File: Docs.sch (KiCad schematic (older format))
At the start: 0 parts

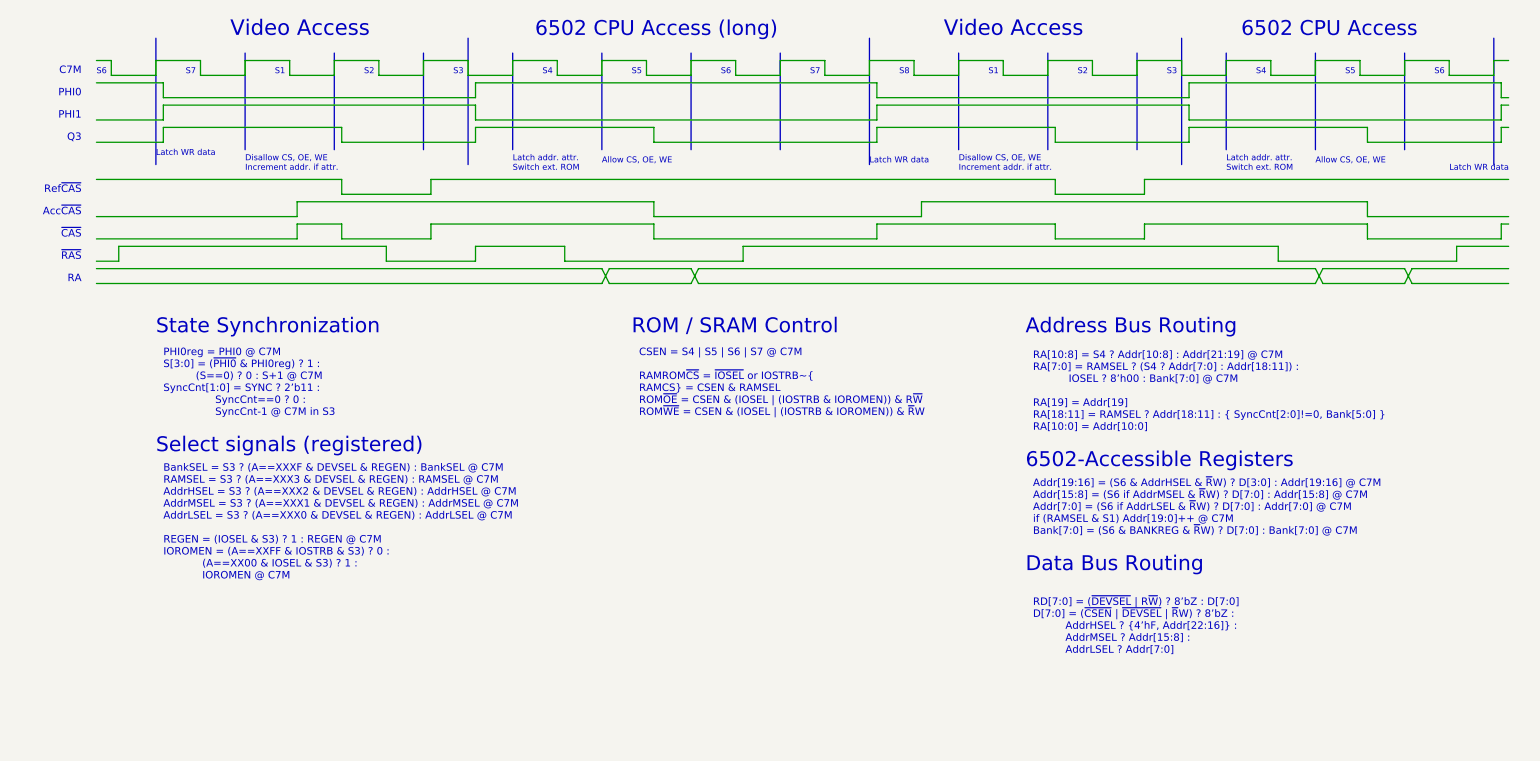
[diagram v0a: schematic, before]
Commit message: Buffered data bus with CPLD
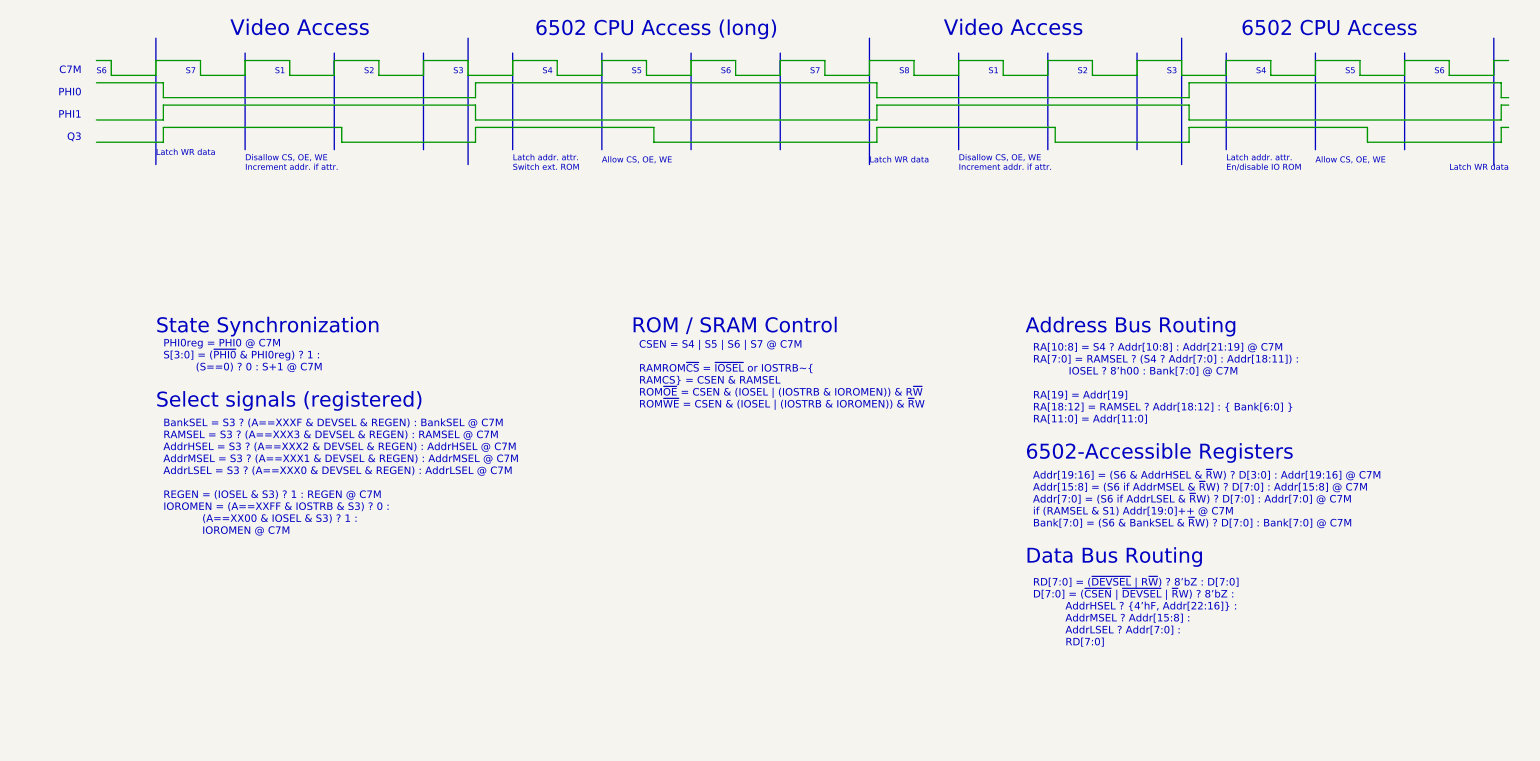
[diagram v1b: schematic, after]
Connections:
- wire segments 176 -> 106
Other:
- note added: "Addr[19:16] = (S6 & AddrHSEL & ~R~W) ? D[3:0] : Addr[19:16] @ C7M\nAddr[15:8] = (S6 if AddrMSEL & ~R~W) ? D[7:0] : Addr[15:8] @ C7M\nAddr[7:0] = (S6 if AddrLSEL & ~R~W) ? D[7:0] : Addr[7:0] @ C7M\nif (RAMSEL & S1) Addr[19:0]++ @ C7M\nBank[7:0] = (S6 & BankSEL & ~R~W) ? D[7:0] : Bank[7:0] @ C7M"
- note added: "Latch addr. attr.\nEn/disable IO ROM"
- note added: "PHI0reg = PHI0 @ C7M\nS[3:0] = (~PHI0~ & PHI0reg) ? 1 : \n (S==0) ? 0 : S+1 @ C7M"
- note added: "RA[10:8] = S4 ? Addr[10:8] : Addr[21:19] @ C7M\nRA[7:0] = RAMSEL ? (S4 ? Addr[7:0] : Addr[18:11]) : \n IOSEL ? 8’h00 : Bank[7:0] @ C7M\n\nRA[19] = Addr[19]\nRA[18:12] = RAMSEL ? Addr[18:12] : { Bank[6:0] }\nRA[11:0] = Addr[11:0]"
- note added: "RD[7:0] = (~DEVSEL~ | R~W~) ? 8’bZ : D[7:0]\nD[7:0] = (~CSEN~ | ~DEVSEL~ | ~R~W) ? 8’bZ :\n AddrHSEL ? {4’hF, Addr[22:16]} : \n AddrMSEL ? Addr[15:8] : \n AddrLSEL ? Addr[7:0] :\n RD[7:0]"
- note removed: "Acc~CAS~"
- note removed: "Addr[19:16] = (S6 & AddrHSEL & ~R~W) ? D[3:0] : Addr[19:16] @ C7M\nAddr[15:8] = (S6 if AddrMSEL & ~R~W) ? D[7:0] : Addr[15:8] @ C7M\nAddr[7:0] = (S6 if AddrLSEL & ~R~W) ? D[7:0] : Addr[7:0] @ C7M\nif (RAMSEL & S1) Addr[19:0]++ @ C7M\nBank[7:0] = (S6 & BANKREG & ~R~W) ? D[7:0] : Bank[7:0] @ C7M"
- note removed: "PHI0reg = PHI0 @ C7M\nS[3:0] = (~PHI0~ & PHI0reg) ? 1 : \n (S==0) ? 0 : S+1 @ C7M\nSyncCnt[1:0] = SYNC ? 2’b11 : \n SyncCnt==0 ? 0 :\n SyncCnt-1 @ C7M in S3"
- note removed: "RA"
- note removed: "RA[10:8] = S4 ? Addr[10:8] : Addr[21:19] @ C7M\nRA[7:0] = RAMSEL ? (S4 ? Addr[7:0] : Addr[18:11]) : \n IOSEL ? 8’h00 : Bank[7:0] @ C7M\n\nRA[19] = Addr[19]\nRA[18:11] = RAMSEL ? Addr[18:11] : { SyncCnt[2:0]!=0, Bank[5:0] }\nRA[10:0] = Addr[10:0]"
- note removed: "RD[7:0] = (~DEVSEL~ | R~W~) ? 8’bZ : D[7:0]\nD[7:0] = (~CSEN~ | ~DEVSEL~ | ~R~W) ? 8’bZ :\n AddrHSEL ? {4’hF, Addr[22:16]} : \n AddrMSEL ? Addr[15:8] : \n AddrLSEL ? Addr[7:0]"
- note removed: "Ref~CAS~"
- note removed: "~CAS~"
- note removed: "~RAS~"
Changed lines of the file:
@@
 Comment4 ""
 $EndDescr
-Wire Wire Line
-	8850 2250 8850 2350
-Wire Wire Line
-	9450 1950 9450 2050
-Wire Wire Line
-	4650 1950 4650 2050
-Wire Wire Line
-	4050 2350 4050 2250
-Text Notes 800  2050 2    50   ~ 0
-Acc~CAS~
-Wire Wire Line
-	3150 1900 2550 1900
 Wire Bus Line
 	4300 950  4300 1600
@@
 Text Notes 4300 1700 0    40   ~ 0
 Allow CS, OE, WE
-Text Notes 3700 1750 0    40   ~ 0
-Latch addr. attr.\nSwitch ext. ROM
-Text Notes 800  2350 2    50   ~ 0
-~RAS~
-Text Notes 800  1900 2    50   ~ 0
-Ref~CAS~
 Text Notes 1500 1100 0    40   ~ 0
 S7
@@
 Text Notes 9900 1100 0    40   ~ 0
 S6
-Text Notes 8500 1750 0    40   ~ 0
-Latch addr. attr.\nSwitch ext. ROM
-Text Notes 6700 1750 0    40   ~ 0
-Disallow CS, OE, WE\nIncrement addr. if attr.
 Wire Wire Line
 	6150 1250 8250 1250
@@
 Wire Bus Line
 	1300 850  1300 1700
-Wire Wire Line
-	7350 1800 7350 1900
-Wire Wire Line
-	3150 1900 3150 1800
-Wire Wire Line
-	2550 1800 2550 1900
-Wire Wire Line
-	3450 2350 3450 2250
-Wire Wire Line
-	2850 2350 3450 2350
-Wire Wire Line
-	2850 2250 2850 2350
-Text Notes 1900 1750 0    40   ~ 0
-Disallow CS, OE, WE\nIncrement addr. if attr.
 Text Notes 1300 1650 0    40   ~ 0
 Latch WR data
@@
 Wire Wire Line
 	5200 1000 5200 1100
-Wire Wire Line
-	9700 2400 9750 2500
-Wire Wire Line
-	9700 2500 9750 2400
-Wire Wire Line
-	9150 2500 9700 2500
-Wire Wire Line
-	9150 2400 9700 2400
-Wire Wire Line
-	9100 2500 9150 2400
-Wire Wire Line
-	9100 2400 9150 2500
-Wire Wire Line
-	9100 2500 4950 2500
-Wire Wire Line
-	4950 2400 9100 2400
-Wire Wire Line
-	4900 2400 4950 2500
-Wire Wire Line
-	4900 2500 4950 2400
-Wire Wire Line
-	4350 2500 4900 2500
-Wire Wire Line
-	4350 2400 4900 2400
-Wire Wire Line
-	4300 2500 4350 2400
-Wire Wire Line
-	4300 2400 4350 2500
-Wire Wire Line
-	900  2400 4300 2400
-Wire Wire Line
-	4300 2500 900  2500
-Text Notes 800  2500 2    50   ~ 0
-RA
-Wire Wire Line
-	2250 2050 2250 1950
-Wire Wire Line
-	2250 1950 4650 1950
-Wire Wire Line
-	5250 2350 5250 2250
-Wire Wire Line
-	5250 2250 8850 2250
-Wire Wire Line
-	1050 2350 1050 2250
-Wire Wire Line
-	1050 2250 2850 2250
-Wire Wire Line
-	900  2350 1050 2350
-Wire Wire Line
-	8850 2350 10050 2350
-Wire Wire Line
-	10050 2350 10050 2250
-Wire Wire Line
-	3450 2250 4050 2250
-Wire Wire Line
-	7950 1900 7950 1800
-Wire Wire Line
-	7950 1900 7350 1900
-Wire Wire Line
-	9450 2100 9450 2200
-Wire Wire Line
-	4650 2100 4650 2200
-Text Notes 800  2200 2    50   ~ 0
-~CAS~
-Wire Wire Line
-	2250 2200 2250 2100
-Wire Wire Line
-	3150 2200 3150 2100
-Wire Wire Line
-	2550 2100 2550 2200
-Wire Wire Line
-	2250 2100 2550 2100
-Wire Wire Line
-	7350 2100 7350 2200
-Wire Wire Line
-	7950 2200 7950 2100
-Wire Wire Line
-	7950 2200 7350 2200
-Wire Wire Line
-	7950 2100 9450 2100
-Wire Wire Line
-	4650 2200 6150 2200
-Wire Wire Line
-	6150 2200 6150 2100
-Wire Wire Line
-	6150 2100 7350 2100
-Wire Wire Line
-	9450 2200 10350 2200
-Wire Wire Line
-	10350 2200 10350 2100
-Wire Wire Line
-	4650 2050 6450 2050
-Wire Wire Line
-	6450 2050 6450 1950
-Wire Wire Line
-	6450 1950 9450 1950
-Wire Wire Line
-	900  2200 2250 2200
-Wire Wire Line
-	900  2050 2250 2050
-Wire Wire Line
-	3150 1800 7350 1800
-Wire Wire Line
-	900  1800 2550 1800
-Wire Wire Line
-	3150 2100 4650 2100
-Wire Wire Line
-	2550 2200 3150 2200
-Wire Wire Line
-	4050 2350 5250 2350
-Text Notes 4550 3400 0    50   ~ 0
+Text Notes 4550 3350 0    50   ~ 0
 CSEN = S4 | S5 | S6 | S7 @ C7M\n\nRAMROM~CS~ = ~IOSEL or IOSTRB~\nRAMCS = CSEN & RAMSEL\nROM~OE~ = CSEN & (IOSEL | (IOSTRB & IOROMEN)) & R~W~\nROM~WE~ = CSEN & (IOSEL | (IOSTRB & IOROMEN)) & ~R~W
-Text Notes 1350 3400 0    50   ~ 0
-PHI0reg = PHI0 @ C7M\nS[3:0] = (~PHI0~ & PHI0reg) ? 1 : \n          (S==0) ? 0 : S+1 @ C7M\nSyncCnt[1:0] = SYNC ? 2’b11 : \n                SyncCnt==0 ? 0 :\n                SyncCnt-1 @ C7M in S3
-Text Notes 7200 3500 0    50   ~ 0
-RA[10:8] = S4 ? Addr[10:8] : Addr[21:19] @ C7M\nRA[7:0] = RAMSEL ? (S4 ? Addr[7:0] : Addr[18:11]) : \n           IOSEL ? 8’h00 : Bank[7:0] @ C7M\n\nRA[19] = Addr[19]\nRA[18:11] = RAMSEL ? Addr[18:11] : { SyncCnt[2:0]!=0, Bank[5:0] }\nRA[10:0] = Addr[10:0]
-Text Notes 1300 3650 0    100  ~ 0
+Text Notes 1350 3100 0    50   ~ 0
+PHI0reg = PHI0 @ C7M\nS[3:0] = (~PHI0~ & PHI0reg) ? 1 : \n          (S==0) ? 0 : S+1 @ C7M
+Text Notes 1300 3350 0    100  ~ 0
 Select signals (registered)
 Text Notes 1300 2850 0    100  ~ 0
@@
 Text Notes 4500 2850 0    100  ~ 0
 ROM / SRAM Control
-Text Notes 1350 4500 0    50   ~ 0
+Text Notes 1350 4200 0    50   ~ 0
 BankSEL = S3 ? (A==XXXF & DEVSEL & REGEN) : BankSEL @ C7M\nRAMSEL = S3 ? (A==XXX3 & DEVSEL & REGEN) : RAMSEL @ C7M\nAddrHSEL = S3 ? (A==XXX2 & DEVSEL & REGEN) : AddrHSEL @ C7M\nAddrMSEL = S3 ? (A==XXX1 & DEVSEL & REGEN) : AddrMSEL @ C7M\nAddrLSEL = S3 ? (A==XXX0 & DEVSEL & REGEN) : AddrLSEL @ C7M\n\nREGEN = (IOSEL & S3) ? 1 : REGEN @ C7M\nIOROMEN = (A==XXFF & IOSTRB & S3) ? 0 :\n            (A==XX00 & IOSEL & S3) ? 1 :\n            IOROMEN @ C7M
 Text Notes 7150 2850 0    100  ~ 0
 Address Bus Routing
-Text Notes 7150 3750 0    100  ~ 0
+Text Notes 7150 3700 0    100  ~ 0
 6502-Accessible Registers
-Text Notes 7200 4200 0    50   ~ 0
-Addr[19:16] = (S6 & AddrHSEL & ~R~W) ? D[3:0] : Addr[19:16] @ C7M\nAddr[15:8] = (S6 if AddrMSEL & ~R~W) ? D[7:0] : Addr[15:8] @ C7M\nAddr[7:0] = (S6 if AddrLSEL & ~R~W) ? D[7:0] : Addr[7:0] @ C7M\nif (RAMSEL & S1) Addr[19:0]++ @ C7M\nBank[7:0] = (S6 & BANKREG & ~R~W) ? D[7:0] : Bank[7:0] @ C7M
-Text Notes 7150 4450 0    100  ~ 0
+Text Notes 7150 4400 0    100  ~ 0
 Data Bus Routing
-Text Notes 7200 5000 0    50   ~ 0
-RD[7:0] = (~DEVSEL~ | R~W~) ? 8’bZ : D[7:0]\nD[7:0] = (~CSEN~ | ~DEVSEL~ | ~R~W) ? 8’bZ :\n          AddrHSEL ? {4’hF, Addr[22:16]} : \n          AddrMSEL ? Addr[15:8] : \n          AddrLSEL ? Addr[7:0]
-Wire Wire Line
-	10350 2100 10400 2100
-Wire Wire Line
-	7950 1800 10400 1800
-Wire Wire Line
-	10050 2250 10400 2250
-Wire Wire Line
-	9450 2050 10400 2050
-Wire Wire Line
-	10400 2400 9750 2400
-Wire Wire Line
-	9750 2500 10400 2500
+Text Notes 7200 4950 0    50   ~ 0
+RD[7:0] = (~DEVSEL~ | R~W~) ? 8’bZ : D[7:0]\nD[7:0] = (~CSEN~ | ~DEVSEL~ | ~R~W) ? 8’bZ :\n          AddrHSEL ? {4’hF, Addr[22:16]} : \n          AddrMSEL ? Addr[15:8] : \n          AddrLSEL ? Addr[7:0] :\n          RD[7:0]
+Wire Wire Line
+	10300 1000 10400 1000
+Wire Wire Line
+	10350 1250 10400 1250
+Wire Wire Line
+	10350 1300 10400 1300
+Wire Wire Line
+	10350 1450 10400 1450
+Text Notes 7200 3450 0    50   ~ 0
+RA[10:8] = S4 ? Addr[10:8] : Addr[21:19] @ C7M\nRA[7:0] = RAMSEL ? (S4 ? Addr[7:0] : Addr[18:11]) : \n           IOSEL ? 8’h00 : Bank[7:0] @ C7M\n\nRA[19] = Addr[19]\nRA[18:12] = RAMSEL ? Addr[18:12] : { Bank[6:0] }\nRA[11:0] = Addr[11:0]
+Text Notes 7200 4150 0    50   ~ 0
+Addr[19:16] = (S6 & AddrHSEL & ~R~W) ? D[3:0] : Addr[19:16] @ C7M\nAddr[15:8] = (S6 if AddrMSEL & ~R~W) ? D[7:0] : Addr[15:8] @ C7M\nAddr[7:0] = (S6 if AddrLSEL & ~R~W) ? D[7:0] : Addr[7:0] @ C7M\nif (RAMSEL & S1) Addr[19:0]++ @ C7M\nBank[7:0] = (S6 & BankSEL & ~R~W) ? D[7:0] : Bank[7:0] @ C7M
 Text Notes 10000 1750 0    40   ~ 0
 Latch WR data
-Wire Wire Line
-	10300 1000 10400 1000
-Wire Wire Line
-	10350 1250 10400 1250
-Wire Wire Line
-	10350 1300 10400 1300
-Wire Wire Line
-	10350 1450 10400 1450
+Text Notes 1900 1750 0    40   ~ 0
+Disallow CS, OE, WE\nIncrement addr. if attr.
+Text Notes 6700 1750 0    40   ~ 0
+Disallow CS, OE, WE\nIncrement addr. if attr.
+Text Notes 3700 1750 0    40   ~ 0
+Latch addr. attr.\nSwitch ext. ROM
+Text Notes 8500 1750 0    40   ~ 0
+Latch addr. attr.\nEn/disable IO ROM
 $EndSCHEMATC

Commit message: Can't fit...
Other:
- note added: "DBEN = ~S2~ @ C7M\n\nRAMROMCS = RAMSEL | IOSEL | (IOSTRB & IOROMEN)\nRAMCS = RAMSEL\nROMCS = RAMROMCSgb & (IOSEL | (IOSTRB & IOROMEN))"
- note added: "RA[19] = Addr[19]\nRA[18:12] = RAMSEL ? Addr[18:12] : Bank[6:0]\nRA[11] = RAMSEL ? Addr[18:12] : A[11]\nRA[10:0] = Addr[11:0]"
- note removed: "CSEN = S4 | S5 | S6 | S7 @ C7M\n\nRAMROM~CS~ = ~IOSEL or IOSTRB~\nRAMCS = CSEN & RAMSEL\nROM~OE~ = CSEN & (IOSEL | (IOSTRB & IOROMEN)) & R~W~\nROM~WE~ = CSEN & (IOSEL | (IOSTRB & IOROMEN)) & ~R~W"
- note removed: "RA[10:8] = S4 ? Addr[10:8] : Addr[21:19] @ C7M\nRA[7:0] = RAMSEL ? (S4 ? Addr[7:0] : Addr[18:11]) : \n IOSEL ? 8’h00 : Bank[7:0] @ C7M\n\nRA[19] = Addr[19]\nRA[18:12] = RAMSEL ? Addr[18:12] : { Bank[6:0] }\nRA[11:0] = Addr[11:0]"
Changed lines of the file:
@@
 Wire Wire Line
 	5200 1000 5200 1100
-Text Notes 4550 3350 0    50   ~ 0
-CSEN = S4 | S5 | S6 | S7 @ C7M\n\nRAMROM~CS~ = ~IOSEL or IOSTRB~\nRAMCS = CSEN & RAMSEL\nROM~OE~ = CSEN & (IOSEL | (IOSTRB & IOROMEN)) & R~W~\nROM~WE~ = CSEN & (IOSEL | (IOSTRB & IOROMEN)) & ~R~W
 Text Notes 1350 3100 0    50   ~ 0
 PHI0reg = PHI0 @ C7M\nS[3:0] = (~PHI0~ & PHI0reg) ? 1 : \n          (S==0) ? 0 : S+1 @ C7M
@@
 Text Notes 1300 2850 0    100  ~ 0
 State Synchronization
-Text Notes 4500 2850 0    100  ~ 0
+Text Notes 4300 2850 0    100  ~ 0
 ROM / SRAM Control
 Text Notes 1350 4200 0    50   ~ 0
@@
 Text Notes 7150 2850 0    100  ~ 0
 Address Bus Routing
-Text Notes 7150 3700 0    100  ~ 0
-6502-Accessible Registers
-Text Notes 7150 4400 0    100  ~ 0
-Data Bus Routing
-Text Notes 7200 4950 0    50   ~ 0
-RD[7:0] = (~DEVSEL~ | R~W~) ? 8’bZ : D[7:0]\nD[7:0] = (~CSEN~ | ~DEVSEL~ | ~R~W) ? 8’bZ :\n          AddrHSEL ? {4’hF, Addr[22:16]} : \n          AddrMSEL ? Addr[15:8] : \n          AddrLSEL ? Addr[7:0] :\n          RD[7:0]
 Wire Wire Line
 	10300 1000 10400 1000
@@
 Wire Wire Line
 	10350 1450 10400 1450
-Text Notes 7200 3450 0    50   ~ 0
-RA[10:8] = S4 ? Addr[10:8] : Addr[21:19] @ C7M\nRA[7:0] = RAMSEL ? (S4 ? Addr[7:0] : Addr[18:11]) : \n           IOSEL ? 8’h00 : Bank[7:0] @ C7M\n\nRA[19] = Addr[19]\nRA[18:12] = RAMSEL ? Addr[18:12] : { Bank[6:0] }\nRA[11:0] = Addr[11:0]
-Text Notes 7200 4150 0    50   ~ 0
-Addr[19:16] = (S6 & AddrHSEL & ~R~W) ? D[3:0] : Addr[19:16] @ C7M\nAddr[15:8] = (S6 if AddrMSEL & ~R~W) ? D[7:0] : Addr[15:8] @ C7M\nAddr[7:0] = (S6 if AddrLSEL & ~R~W) ? D[7:0] : Addr[7:0] @ C7M\nif (RAMSEL & S1) Addr[19:0]++ @ C7M\nBank[7:0] = (S6 & BankSEL & ~R~W) ? D[7:0] : Bank[7:0] @ C7M
+Text Notes 7200 3200 0    50   ~ 0
+RA[19] = Addr[19]\nRA[18:12] = RAMSEL ? Addr[18:12] : Bank[6:0]\nRA[11] = RAMSEL ? Addr[18:12] : A[11]\nRA[10:0] = Addr[11:0]
 Text Notes 10000 1750 0    40   ~ 0
 Latch WR data
@@
 Text Notes 8500 1750 0    40   ~ 0
 Latch addr. attr.\nEn/disable IO ROM
+Text Notes 7150 3450 0    100  ~ 0
+6502-Accessible Registers
+Text Notes 7150 4150 0    100  ~ 0
+Data Bus Routing
+Text Notes 7200 4700 0    50   ~ 0
+RD[7:0] = (~DEVSEL~ | R~W~) ? 8’bZ : D[7:0]\nD[7:0] = (~CSEN~ | ~DEVSEL~ | ~R~W) ? 8’bZ :\n          AddrHSEL ? {4’hF, Addr[22:16]} : \n          AddrMSEL ? Addr[15:8] : \n          AddrLSEL ? Addr[7:0] :\n          RD[7:0]
+Text Notes 7200 3900 0    50   ~ 0
+Addr[19:16] = (S6 & AddrHSEL & ~R~W) ? D[3:0] : Addr[19:16] @ C7M\nAddr[15:8] = (S6 if AddrMSEL & ~R~W) ? D[7:0] : Addr[15:8] @ C7M\nAddr[7:0] = (S6 if AddrLSEL & ~R~W) ? D[7:0] : Addr[7:0] @ C7M\nif (RAMSEL & S1) Addr[19:0]++ @ C7M\nBank[7:0] = (S6 & BankSEL & ~R~W) ? D[7:0] : Bank[7:0] @ C7M
+Text Notes 4350 3300 0    50   ~ 0
+DBEN = ~S2~ @ C7M\n\nRAMROMCS = RAMSEL | IOSEL | (IOSTRB & IOROMEN)\nRAMCS = RAMSEL\nROMCS = RAMROMCSgb & (IOSEL | (IOSTRB & IOROMEN))
 $EndSCHEMATC

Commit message: Lots of state machine work
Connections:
- wire segments 106 -> 124
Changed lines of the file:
@@
 Text Notes 4350 3300 0    50   ~ 0
 DBEN = ~S2~ @ C7M\n\nRAMROMCS = RAMSEL | IOSEL | (IOSTRB & IOROMEN)\nRAMCS = RAMSEL\nROMCS = RAMROMCSgb & (IOSEL | (IOSTRB & IOROMEN))
+Wire Wire Line
+	3700 1850 3750 1950
+Wire Wire Line
+	3750 1950 6700 1950
+Wire Wire Line
+	6700 1950 6750 1850
+Wire Wire Line
+	6750 1850 8500 1850
+Wire Wire Line
+	8500 1850 8550 1950
+Wire Wire Line
+	8550 1950 10400 1950
+Wire Wire Line
+	1950 1850 3700 1850
+Wire Wire Line
+	1950 1850 1900 1950
+Wire Wire Line
+	1900 1950 900  1950
+Wire Wire Line
+	4300 2000 4350 2100
+Wire Wire Line
+	4350 2100 7300 2100
+Wire Wire Line
+	7300 2100 7350 2000
+Wire Wire Line
+	7350 2000 9100 2000
+Wire Wire Line
+	9100 2000 9150 2100
+Wire Wire Line
+	9150 2100 10400 2100
+Wire Wire Line
+	2550 2000 4300 2000
+Wire Wire Line
+	2550 2000 2500 2100
+Wire Wire Line
+	900  2100 2500 2100
 $EndSCHEMATC
